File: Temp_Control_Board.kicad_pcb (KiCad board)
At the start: 2 copper layers, 111.8 x 50.8 mm, 38 parts, among them J1 OVEN_INTERFACE, J2 OLED, J3 USB_B_Micro, J4 MICROSD, U1 ESP-WROOM-32, U2 AZ1117EH-3.3TRG1, U3 ROTARY_ENC_PEC12R, U4 FT232RLREEL, U5 MAX31855KASA

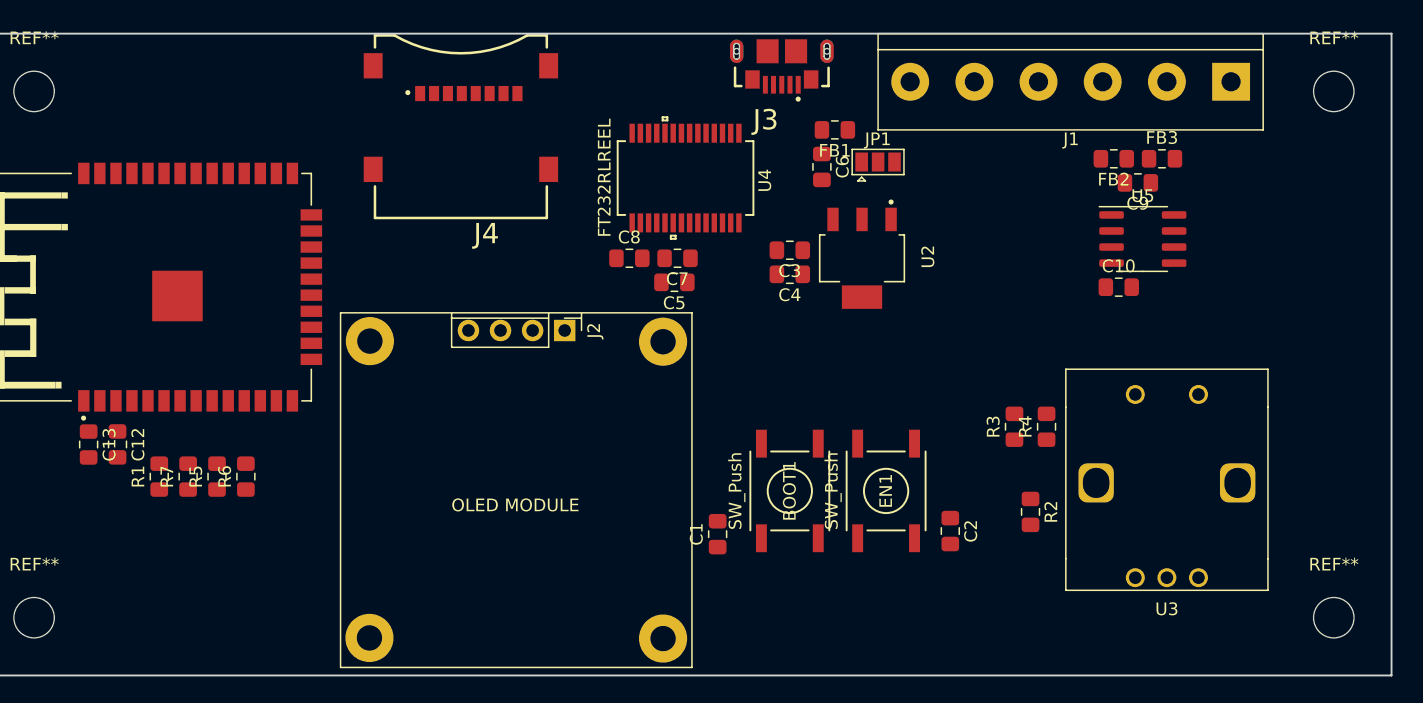
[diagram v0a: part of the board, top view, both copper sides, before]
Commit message: pro: set track widths
pcb: routed power and ground
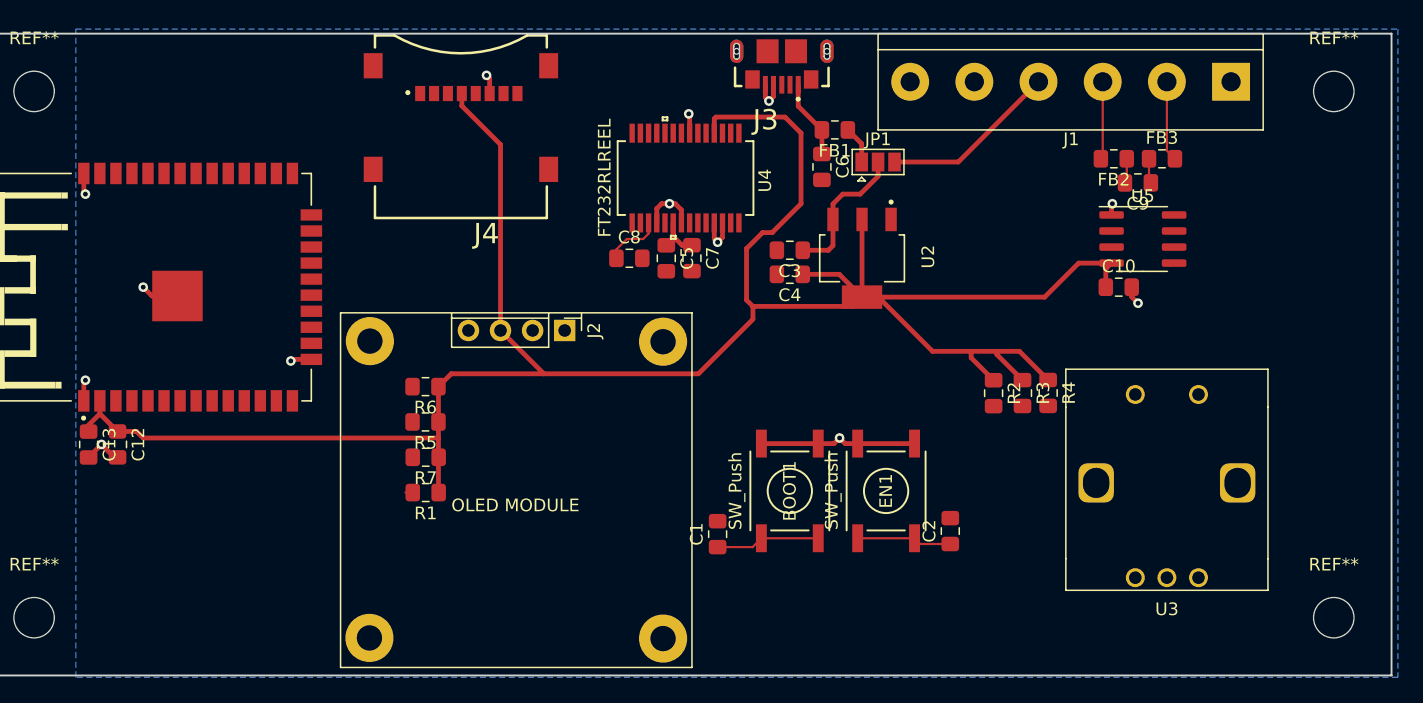
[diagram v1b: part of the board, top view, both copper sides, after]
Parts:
- BOOT1, EN1: footprint TACTILE_SWITCH:PTS645SK43SMTR92LFS -> TACTILE_SWITCH:PTS645SK43SMTR92LF-CONNECTED
- moved R1 21.1 mm to (103.9, 140.5), turned to 180 degrees
- moved R7 18.9 mm to (103.9, 137.7), turned to 180 degrees
- moved R5 17.1 mm to (103.9, 134.9), turned to 180 degrees
- moved R6 15.9 mm to (103.9, 132.1), turned to 180 degrees
- moved R2 9.84 mm to (148.8, 132.6)
- moved R3 2.74 mm to (151.1, 132.6), turned to 270 degrees
- moved R4 2.68 mm to (153.2, 132.6), turned to 270 degrees
- moved C5 2.01 mm to (122.9, 121.9), turned to 270 degrees
- moved C7 1.14 mm to (125.0, 121.9), turned to 270 degrees
- turned C2 to 90 degrees
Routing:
- net +3V3: track 0.00 -> 183.6 mm
- net GND: track 0.00 -> 39.8 mm, vias 0 -> 13
- net +5V: track 0.00 -> 16.3 mm
- net VCONN: track 0.00 -> 14.0 mm
- net EN: track 0.00 -> 8.85 mm
- net BOOT: track 0.00 -> 8.25 mm
- net /TC+: track 0.00 -> 6.36 mm
- net /VBUS: track 0.00 -> 6.25 mm
- net /TC-: track 0.00 -> 6.16 mm
- net /FT_3V3OUT: track 0.00 -> 4.61 mm
- net VUSB: track 0.00 -> 2.99 mm
- net MAX_TX-: track 0.00 -> 1.97 mm
- net MAX_TC+: track 0.00 -> 1.97 mm
- added copper zone on B.Cu, net GND
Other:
- net class Default: clearance 0.2 -> 0.2032; trace_width 0.25 -> 0.1778; via_dia 0.8 -> 0.762; via_drill 0.4 -> 0.381
- net class Power added: clearance 0.2032, trace_width 0.381, via_dia 0.762, via_drill 0.381
- rule trace_clearance: 0.2 -> 0.2032
- rule trace_min: 0.2 -> 0.1778

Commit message: ORD airport
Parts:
- moved C2 65.9 mm to (80.3, 153.4), turned to 180 degrees
- moved BOOT1 56.4 mm to (85.2, 109.9)
- moved C1 56.4 mm to (79.5, 113.3)
- moved EN1 53.9 mm to (87.5, 151.0), turned to 0 degrees
- moved R1 25.9 mm to (80.3, 151.1), turned to 0 degrees
- moved R7 24.9 mm to (128.5, 134.1), turned to 270 degrees
- moved R5 21.9 mm to (125.7, 134.1), turned to 270 degrees
- moved R6 19.2 mm to (122.9, 134.1), turned to 270 degrees
- moved R4 16.4 mm to (150.6, 116.3), turned to 0 degrees
- moved C8 16.4 mm to (125.3, 106.4), turned to 180 degrees
- moved C7 16.1 mm to (120.4, 106.4), turned to 90 degrees
- moved C5 15.5 mm to (122.4, 106.4), turned to 90 degrees
- moved R3 14.2 mm to (150.6, 118.4), turned to 0 degrees
- moved R2 12.1 mm to (150.6, 120.7), turned to 0 degrees
- moved C12 10.4 mm to (79.5, 147.1)
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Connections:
- U1 pad 29: Net-(U1-Pad29) -> FT_CTS
- U1 pad 30: Net-(U1-Pad30) -> FT_PWREN
- U1 pad 31: Net-(U1-Pad31) -> FT_RTS
- U1 pad 6: FT_RTS -> Net-(U1-Pad6)
- U1 pad 7: FT_CTS -> Net-(U1-Pad7)
- U1 pad 9: FT_PWREN -> Net-(U1-Pad9)
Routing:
- net +3V3: track 183.6 -> 138.1 mm
- net ROT_CHB: track 0.00 -> 38.8 mm
- net ROT_CHA: track 0.00 -> 35.0 mm
- net ROT_SW1: track 0.00 -> 22.7 mm
- net +5V: track 16.3 -> 35.1 mm
- net /D-: track 0.00 -> 12.0 mm
- net GND: track 39.8 -> 51.1 mm, vias 13 -> 21
- net /D+: track 0.00 -> 10.8 mm
- net MAX_TC+: track 1.97 -> 10.5 mm
- net EN: track 8.85 -> 17.0 mm
- net MAX_TX-: track 1.97 -> 4.36 mm

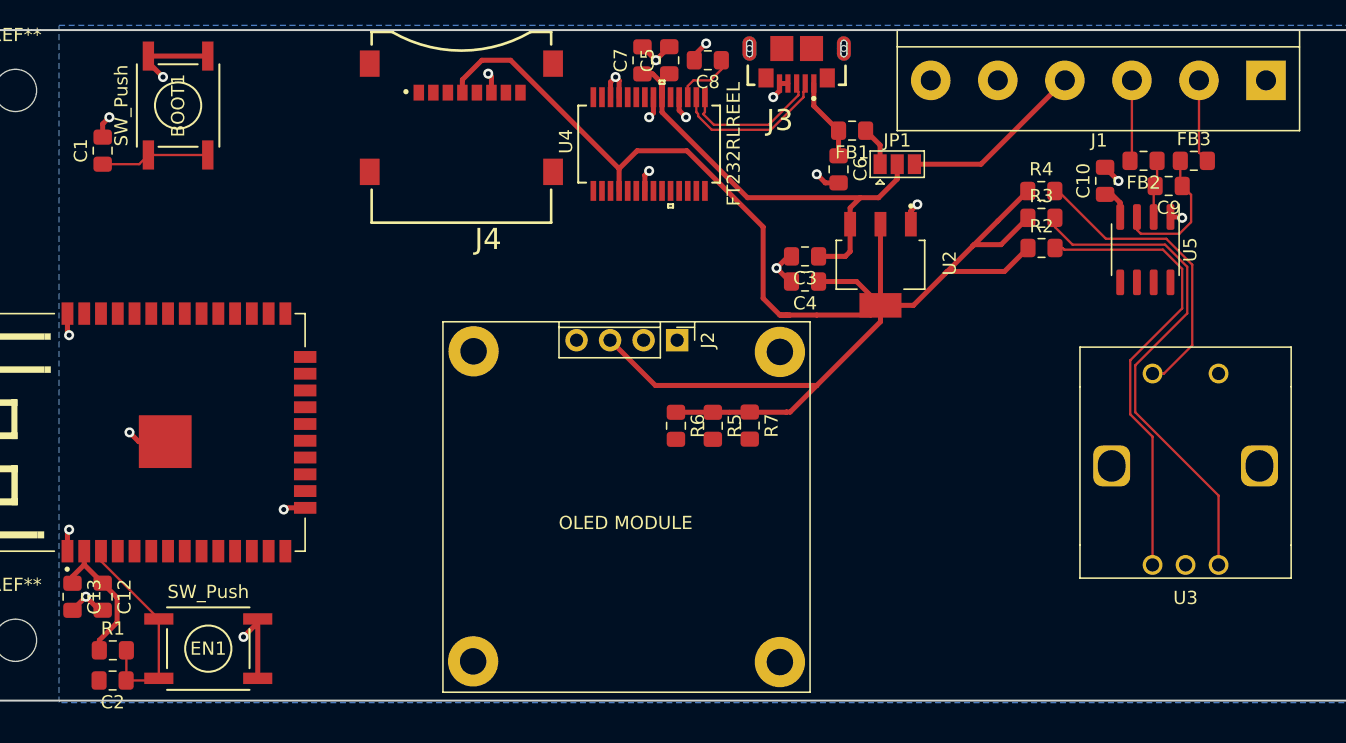
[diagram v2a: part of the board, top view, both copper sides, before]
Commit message: After airport. Routed, needs touching up.
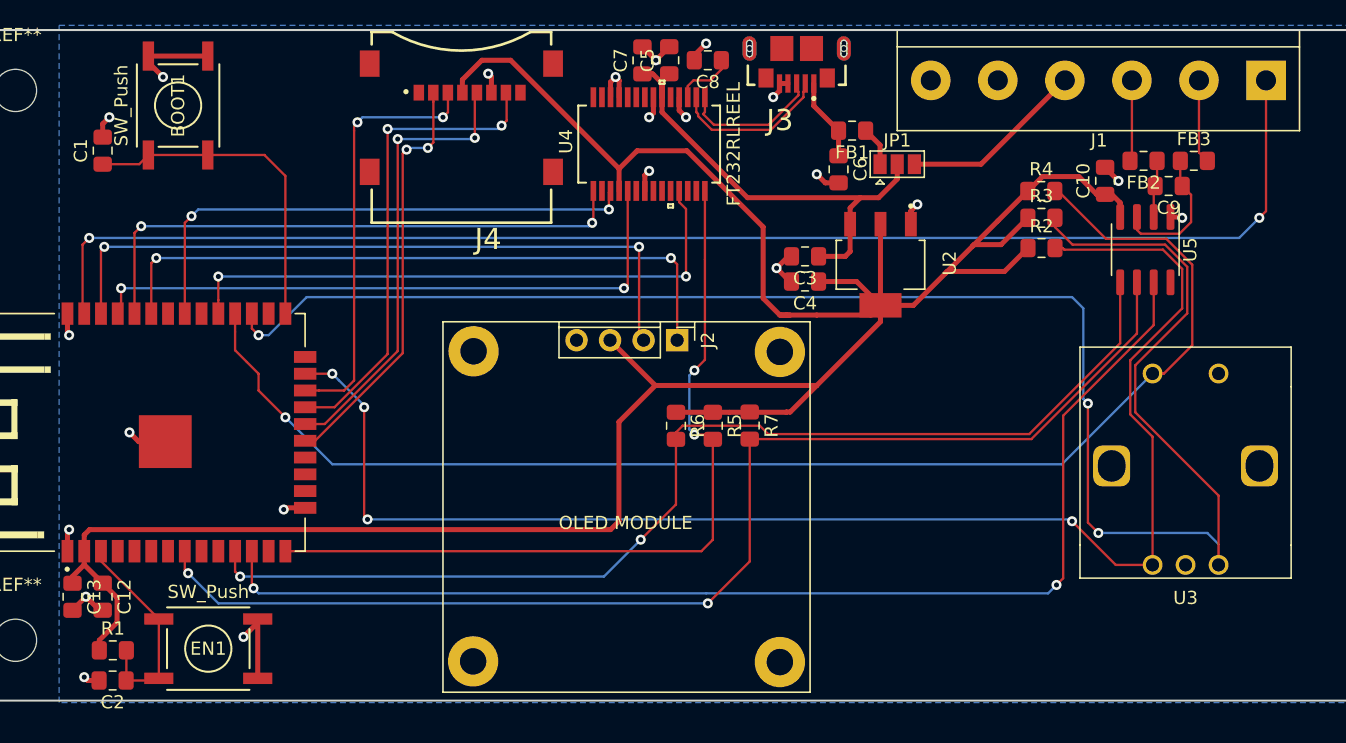
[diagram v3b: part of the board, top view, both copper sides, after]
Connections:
- J4 pad 10: Net-(J4-Pad10) -> (no net)
- J4 pad 11: Net-(J4-Pad10) -> (no net)
- J4 pad 12: Net-(J4-Pad10) -> (no net)
- J4 pad 9: Net-(J4-Pad10) -> (no net)
- U1 pad 14: Net-(U1-Pad14) -> FT_PWREN
- U1 pad 30: FT_PWREN -> Net-(U1-Pad30)
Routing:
- net RELAY+: track 0.00 -> 105.9 mm, vias 0 -> 2
- net ROT_CHB: track 38.8 -> 133.2 mm, vias 0 -> 3
- net MAX_CSN: track 0.00 -> 92.4 mm, vias 0 -> 2
- net MAX_SO: track 0.00 -> 90.1 mm, vias 0 -> 2
- net MAX_SCK: track 0.00 -> 84.4 mm, vias 0 -> 2
- net ROT_SW1: track 22.7 -> 102.2 mm, vias 0 -> 1
- net ROT_CHA: track 35.0 -> 110.1 mm, vias 0 -> 4
- net FT_PWREN: track 0.00 -> 61.4 mm, vias 0 -> 2
- net +3V3: track 138.1 -> 198.5 mm
- net OLED_SCL: track 0.00 -> 52.9 mm, vias 0 -> 2
- net OLED_SDA: track 0.00 -> 49.8 mm, vias 0 -> 2
- net FT_RX: track 0.00 -> 47.6 mm, vias 0 -> 2
- net FT_CTS: track 0.00 -> 44.9 mm, vias 0 -> 2
- net FT_TX: track 0.00 -> 43.6 mm, vias 0 -> 2
- net FT_RTS: track 0.00 -> 40.9 mm, vias 0 -> 2
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
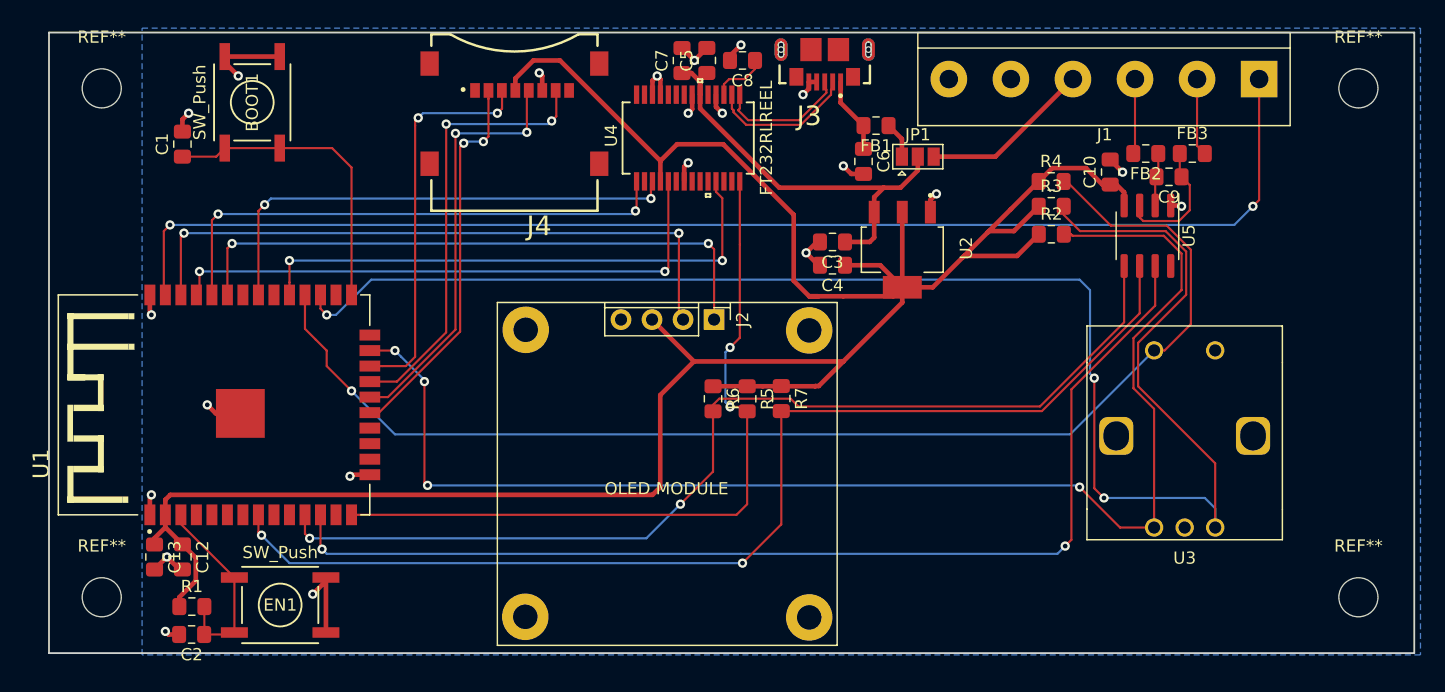
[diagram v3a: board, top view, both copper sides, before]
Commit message: pcb: Finished Routing
    -Touched up some traces
    -Made silkscreen presentable
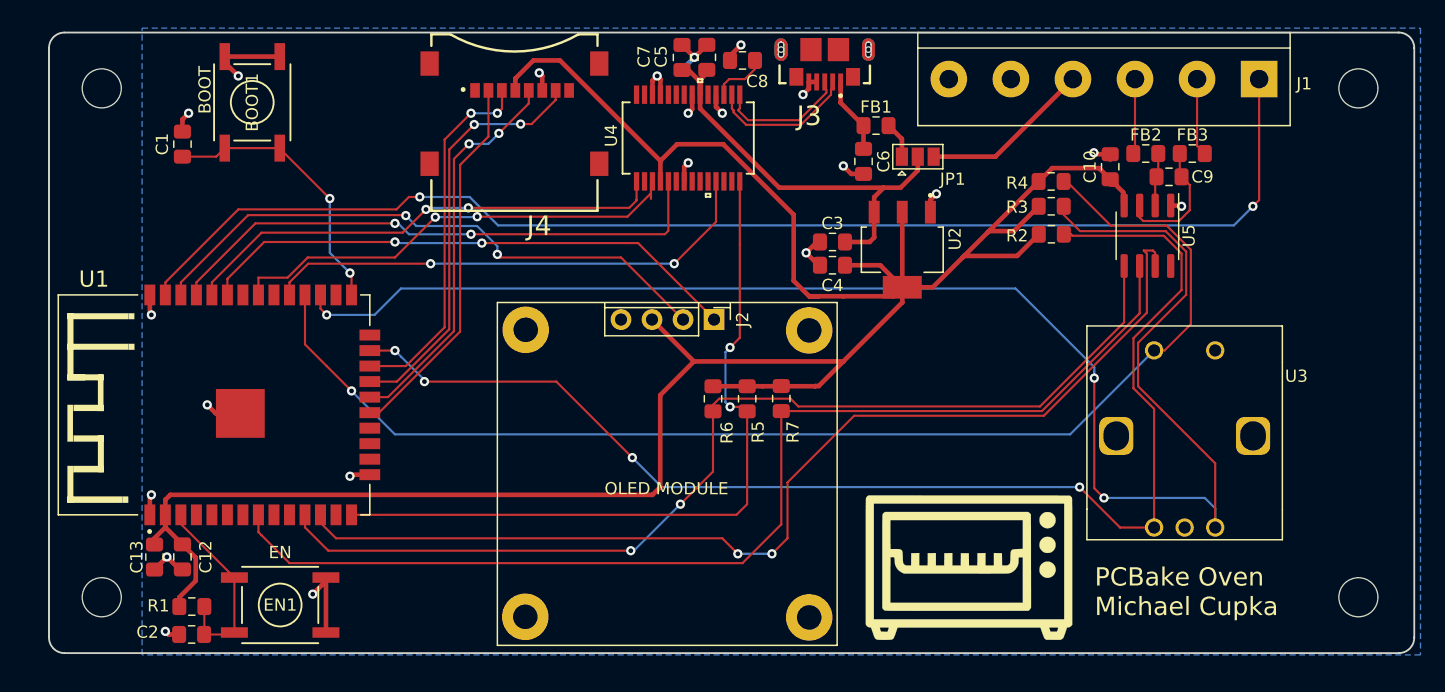
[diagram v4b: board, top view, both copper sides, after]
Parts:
- added G***: LOGO, ART:oven, F.Cu at (143.9, 148.0)
- BOOT1: value SW_Push -> BOOT
- EN1: value SW_Push -> EN
- moved C10 0.44 mm to (155.4, 115.1)
- moved C5 0.25 mm to (122.4, 106.2)
- moved C7 0.25 mm to (120.4, 106.2)
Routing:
- net ROT_CHA: track 110.1 -> 105.3 mm
- net OLED_SDA: track 49.8 -> 45.1 mm
- net ROT_CHB: track 133.2 -> 129.1 mm
- net OLED_SCL: track 52.9 -> 48.8 mm
- net FT_CTS: track 44.9 -> 41.3 mm
- net FT_TX: track 43.6 -> 40.1 mm
- net MAX_SO: track 90.1 -> 87.5 mm
- net FT_RTS: track 40.9 -> 38.3 mm
- net BOOT: track 25.2 -> 22.7 mm, vias 0 -> 2
- net SD_SCK: track 34.7 -> 32.3 mm
- net SD_DI: track 32.3 -> 30.0 mm
- net SD_DO: track 36.4 -> 34.2 mm
- net FT_RX: track 47.6 -> 46.2 mm
- net SD_CS: track 31.7 -> 30.8 mm, vias 2 -> 0
- net GND: track 52.4 -> 53.2 mm
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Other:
- outline, holes or cut-outs redrawn
- board text added: "PCBake Oven Michael Cupka"
